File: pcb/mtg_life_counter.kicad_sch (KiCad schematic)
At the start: 41 parts, among them J1 USB C 4907, J2 ICSP, J3 TP_UART, SW1 SW_SPST, SW2 SW_SPST, U1 ATmega328P-AU, Y1 16MHz

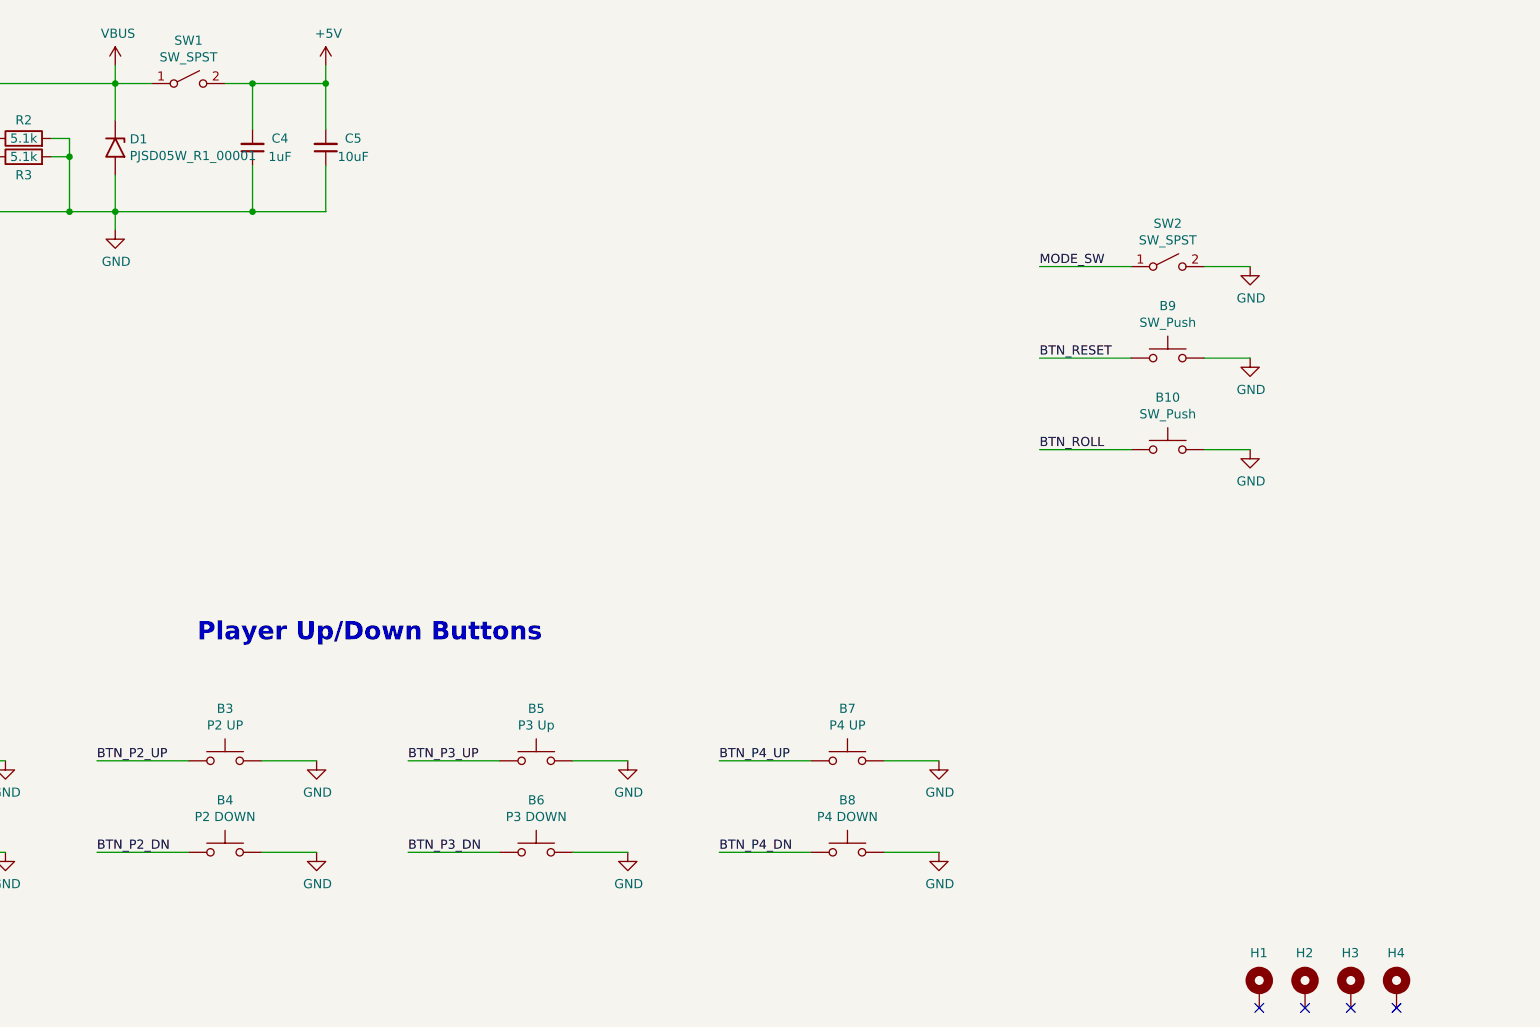
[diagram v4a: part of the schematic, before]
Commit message: start to route display traces
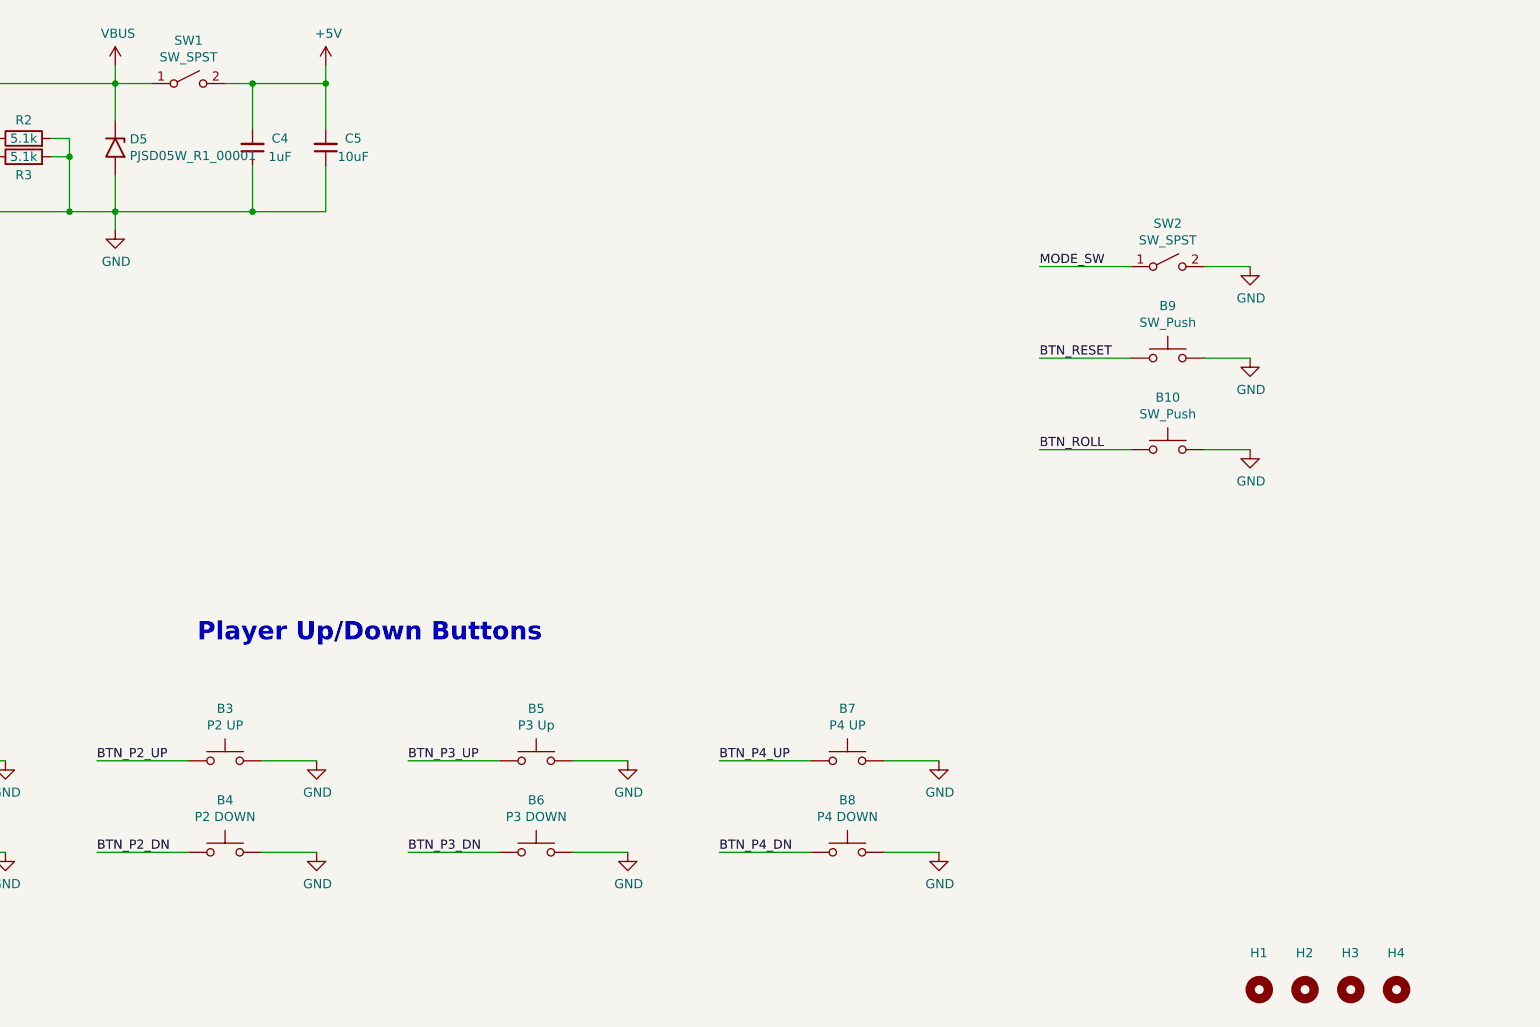
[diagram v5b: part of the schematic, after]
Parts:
- H1, H2, H3, H4: footprint MountingHole:MountingHole_3.2mm_M3_Pad_Via -> MountingHole:MountingHole_3.2mm_M3; symbol Mechanical:MountingHole_Pad -> Mechanical:MountingHole; now left out of the parts list
- renumbered D1 to D5
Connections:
- no-connect marks 8 -> 4
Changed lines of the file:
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@@
 	)
 	(no_connect
-		(at 243.84 255.27)
-	)
-	(no_connect
 		(at 69.85 78.74)
 	)
 	(no_connect
-		(at 256.54 255.27)
-	)
-	(no_connect
 		(at 69.85 76.2)
 	)
@@
 	)
 	(no_connect
-		(at 237.49 255.27)
-	)
-	(no_connect
 		(at 69.85 66.04)
 	)
-	(no_connect
-		(at 250.19 255.27)
-	)
 	(wire
 		(pts
@@
 	)
 	(symbol
-		(lib_id "Mechanical:MountingHole_Pad")
+		(lib_id "Mechanical:MountingHole")
 		(at 237.49 252.73 0)
 		(unit 1)
 		(exclude_from_sim no)
-		(in_bom yes)
+		(in_bom no)
 		(on_board yes)
 		(dnp no)
@@
 			)
 		)
-		(property "Footprint" "MountingHole:MountingHole_3.2mm_M3_Pad_Via"
+		(property "Footprint" "MountingHole:MountingHole_3.2mm_M3"
 			(at 237.49 252.73 0)
 			(effects
@@
 			)
 		)
-		(property "Description" ""
+		(property "Description" "Mounting Hole without connection"
 			(at 237.49 252.73 0)
 			(effects
@@
 			)
 		)
-		(pin "1"
-		)
 		(instances
 			(project "mtg_life_counter"
@@
 	)
 	(symbol
-		(lib_id "Mechanical:MountingHole_Pad")
+		(lib_id "Mechanical:MountingHole")
 		(at 256.54 252.73 0)
 		(unit 1)
 		(exclude_from_sim no)
-		(in_bom yes)
+		(in_bom no)
 		(on_board yes)
 		(dnp no)
@@
 			)
 		)
-		(property "Footprint" "MountingHole:MountingHole_3.2mm_M3_Pad_Via"
+		(property "Footprint" "MountingHole:MountingHole_3.2mm_M3"
 			(at 256.54 252.73 0)
 			(effects
@@
 			)
 		)
-		(property "Description" ""
+		(property "Description" "Mounting Hole without connection"
 			(at 256.54 252.73 0)
 			(effects
@@
 			)
 		)
-		(pin "1"
-		)
 		(instances
 			(project "mtg_life_counter"
@@
 	)
 	(symbol
-		(lib_id "Mechanical:MountingHole_Pad")
+		(lib_id "Mechanical:MountingHole")
 		(at 250.19 252.73 0)
 		(unit 1)
 		(exclude_from_sim no)
-		(in_bom yes)
+		(in_bom no)
 		(on_board yes)
 		(dnp no)
@@
 			)
 		)
-		(property "Footprint" "MountingHole:MountingHole_3.2mm_M3_Pad_Via"
+		(property "Footprint" "MountingHole:MountingHole_3.2mm_M3"
 			(at 250.19 252.73 0)
 			(effects
@@
 			)
 		)
-		(property "Description" ""
+		(property "Description" "Mounting Hole without connection"
 			(at 250.19 252.73 0)
 			(effects
@@
 			)
 		)
-		(pin "1"
-		)
 		(instances
 			(project "mtg_life_counter"
@@
 	)
 	(symbol
-		(lib_id "Mechanical:MountingHole_Pad")
+		(lib_id "Mechanical:MountingHole")
 		(at 243.84 252.73 0)
 		(unit 1)
 		(exclude_from_sim no)
-		(in_bom yes)
+		(in_bom no)
 		(on_board yes)
 		(dnp no)
@@
 			)
 		)
-		(property "Footprint" "MountingHole:MountingHole_3.2mm_M3_Pad_Via"
+		(property "Footprint" "MountingHole:MountingHole_3.2mm_M3"
 			(at 243.84 252.73 0)
 			(effects
@@
 			)
 		)
-		(property "Description" ""
+		(property "Description" "Mounting Hole without connection"
 			(at 243.84 252.73 0)
 			(effects
@@
 			)
 		)
-		(pin "1"
-		)
 		(instances
 			(project "mtg_life_counter"
@@
 		(on_board yes)
 		(dnp no)
-		(property "Reference" "D1"
+		(property "Reference" "D5"
 			(at 80.7466 134.7216 90)
 			(effects
@@
 			(project "mtg_life_counter"
 				(path "/1883df74-0bd5-446c-9076-f848bb3cfebf"
-					(reference "D1")
+					(reference "D5")
 					(unit 1)
 				)

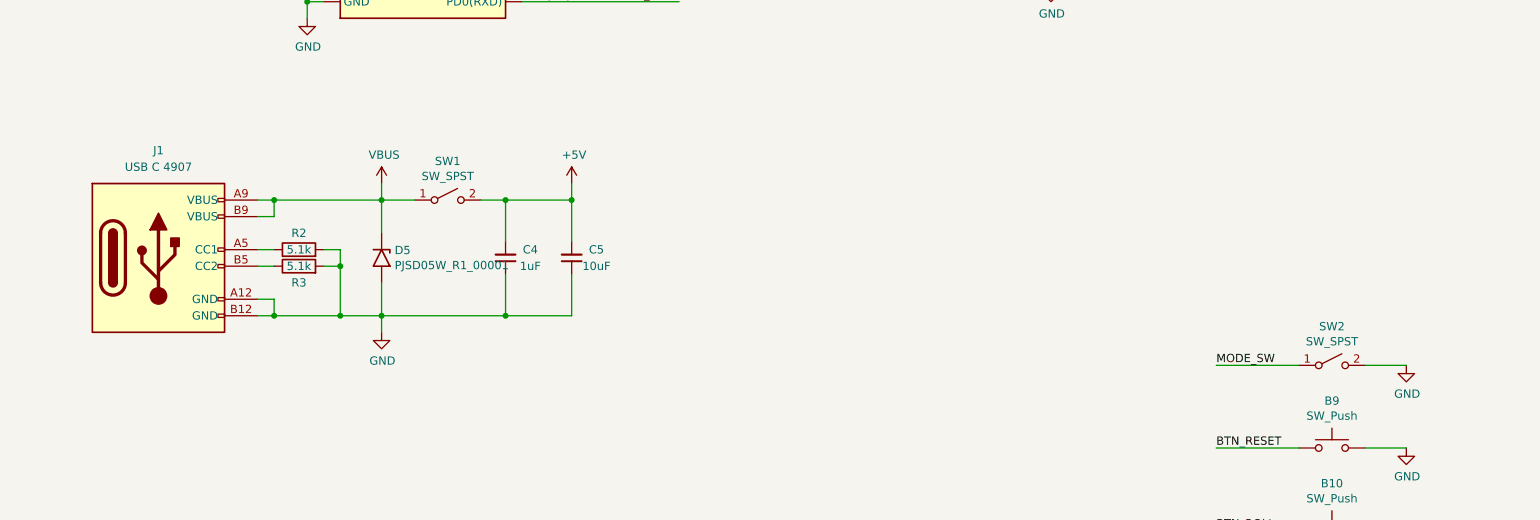
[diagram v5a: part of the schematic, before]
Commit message: switch to all smd components
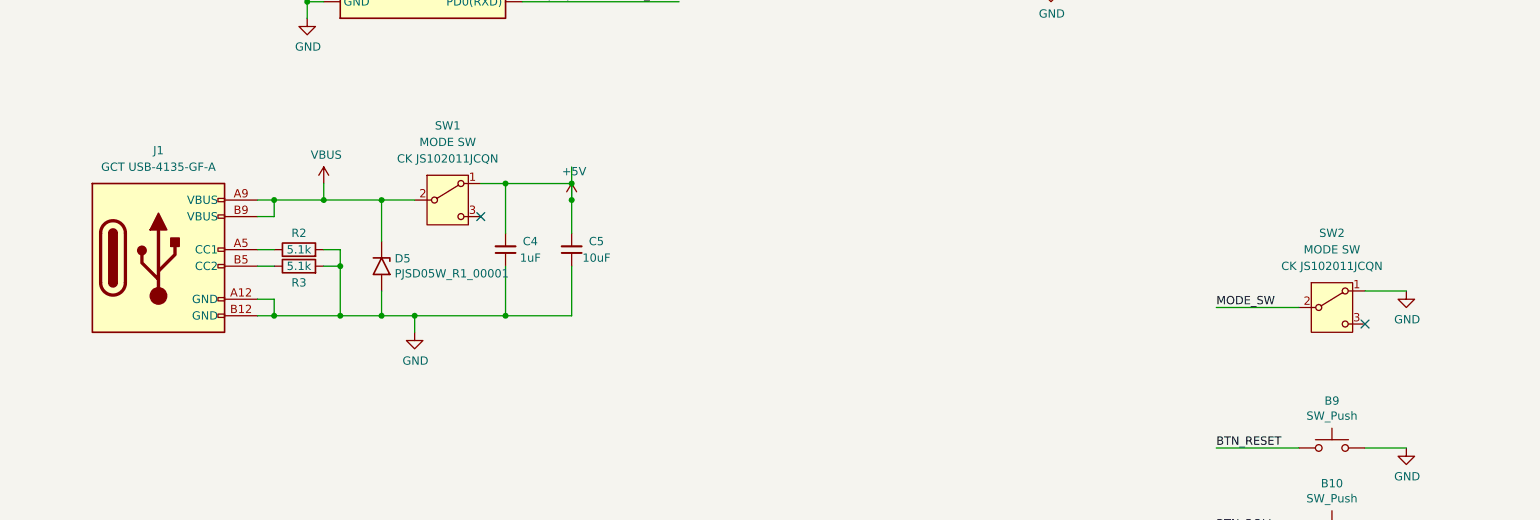
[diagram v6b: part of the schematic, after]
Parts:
- removed SW1, SW2: SW_SPST, Button_Switch_THT:SW_Slide_SPDT_Straight_CK_OS102011MS2Q, symbol Switch:SW_SPST
- added SW1, SW2: MODE SW, mtg_life_counter:SW_SPDT_CK_JS102011JCQN, symbol Switch:SW_SPDT
- B1, B10, B2, B3, B4, B5, B6, B7, B8, B9: footprint mtg_life_counter:B3F_12mm -> mtg_life_counter:SW_SPST_WE_WS-TASV_12mm_Tac
- J1: value USB C 4907 -> GCT USB-4135-GF-A; footprint mtg_life_counter:4907_USB_C_PowerOnly -> Connector_USB:USB_C_Receptacle_GCT_USB4135-GF-A_6P_TopMnt_Horizontal
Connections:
- net +5V: now also SW1.1 (A)
- net GND: now also SW2.1 (A)
- net MODE_SW: now also SW2.2 (B)
- net VBUS: now also SW1.2 (B)
- no-connect marks 4 -> 6
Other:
- moved on the sheet: C4, C5, D5

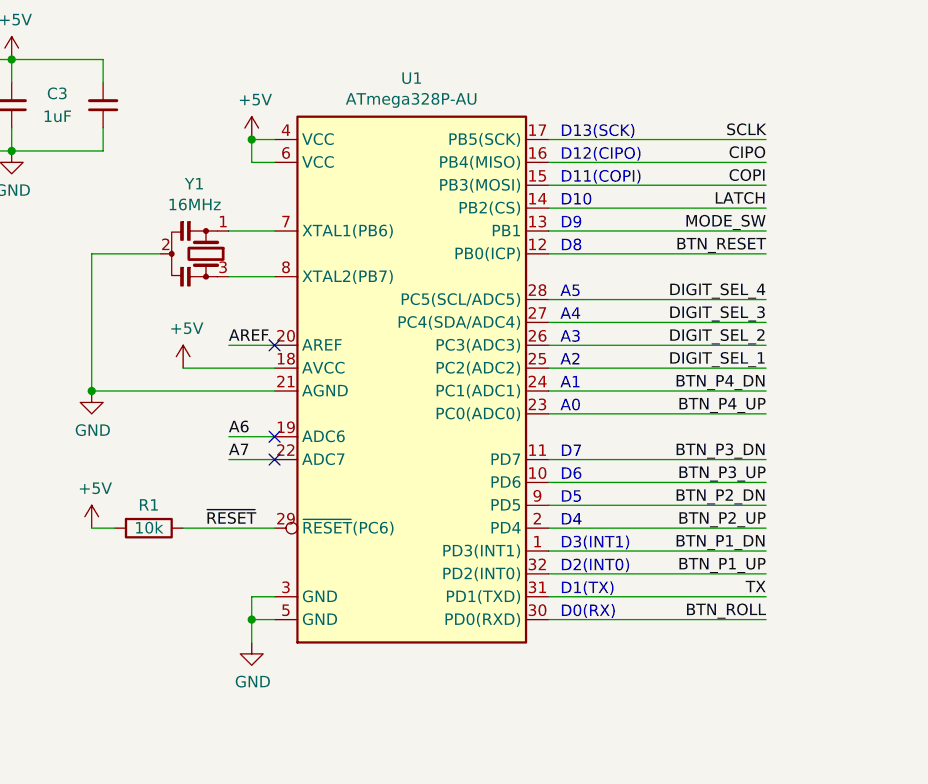
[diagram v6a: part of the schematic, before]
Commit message: continue layout. improve 3d model
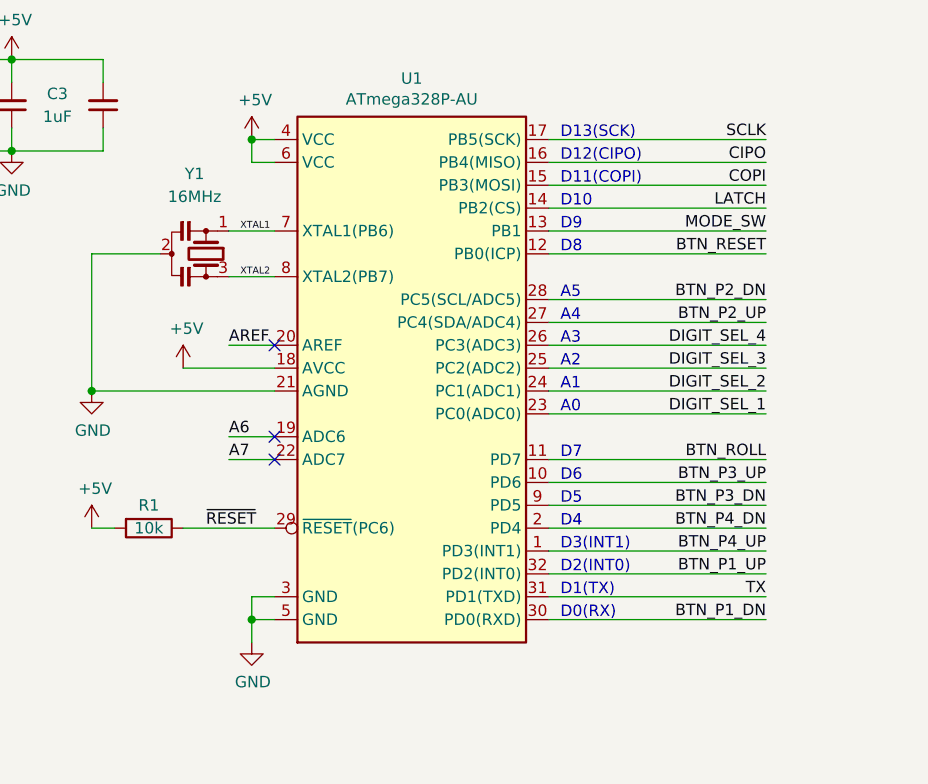
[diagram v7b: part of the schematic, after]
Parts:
- Y1: footprint Crystal:Resonator_SMD-3Pin_7.2x3.0mm -> Crystal:Resonator_SMD_Murata_CSTxExxV-3Pin_3.0x1.1mm_HandSoldering
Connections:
- net BTN_P1_DN: now also U1.30 (PD0(RXD)); no longer U1.1 (PD3(INT1))
- net BTN_P2_DN: now also U1.28 (PC5(SCL/ADC5)); no longer U1.9 (PD5)
- net BTN_P2_UP: now also U1.27 (PC4(SDA/ADC4)); no longer U1.2 (PD4)
- net BTN_P3_DN: now also U1.9 (PD5); no longer U1.11 (PD7)
- net BTN_P4_DN: now also U1.2 (PD4); no longer U1.24 (PC1(ADC1))
- net BTN_P4_UP: now also U1.1 (PD3(INT1)); no longer U1.23 (PC0(ADC0))
- net BTN_ROLL: now also U1.11 (PD7); no longer U1.30 (PD0(RXD))
- net DIGIT_SEL_1: now also U1.23 (PC0(ADC0)); no longer U1.25 (PC2(ADC2))
- net DIGIT_SEL_2: now also U1.24 (PC1(ADC1)); no longer U1.26 (PC3(ADC3))
- net DIGIT_SEL_3: now also U1.25 (PC2(ADC2)); no longer U1.27 (PC4(SDA/ADC4))
- net DIGIT_SEL_4: now also U1.26 (PC3(ADC3)); no longer U1.28 (PC5(SCL/ADC5))
- net XTAL1: now reaches U1.7 (XTAL1(PB6)), Y1.1
- net XTAL2: now reaches U1.8 (XTAL2(PB7)), Y1.3
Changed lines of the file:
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@@
 	)
 	(label "BTN_P1_DN"
-		(at 124.46 88.9 180)
+		(at 124.46 96.52 180)
 		(effects
 			(font
@@
 	)
 	(label "BTN_P2_UP"
-		(at 124.46 86.36 180)
+		(at 124.46 63.5 180)
 		(effects
 			(font
@@
 	)
 	(label "DIGIT_SEL_3"
-		(at 124.46 63.5 180)
+		(at 124.46 68.58 180)
 		(effects
 			(font
@@
 	)
 	(label "BTN_P4_DN"
-		(at 124.46 71.12 180)
+		(at 124.46 86.36 180)
 		(effects
 			(font
@@
 	)
 	(label "DIGIT_SEL_1"
-		(at 124.46 68.58 180)
+		(at 124.46 73.66 180)
 		(effects
 			(font
@@
 		)
 	)
+	(label "XTAL2"
+		(at 66.04 58.42 0)
+		(effects
+			(font
+				(size 0.762 0.762)
+			)
+			(justify left bottom)
+		)
+	)
 	(label "LATCH"
 		(at 314.96 147.32 0)
@@
 	)
 	(label "DIGIT_SEL_4"
-		(at 124.46 60.96 180)
+		(at 124.46 66.04 180)
 		(effects
 			(font
@@
 		)
 	)
+	(label "XTAL1"
+		(at 66.04 53.34 0)
+		(effects
+			(font
+				(size 0.762 0.762)
+			)
+			(justify left bottom)
+		)
+	)
 	(label "BTN_P4_DN"
 		(at 162.56 233.68 0)
@@
 	)
 	(label "BTN_ROLL"
-		(at 124.46 96.52 180)
+		(at 124.46 78.74 180)
 		(effects
 			(font
@@
 	)
 	(label "BTN_P4_UP"
-		(at 124.46 73.66 180)
+		(at 124.46 88.9 180)
 		(effects
 			(font
@@
 	)
 	(label "BTN_P3_DN"
-		(at 124.46 78.74 180)
+		(at 124.46 83.82 180)
 		(effects
 			(font
@@
 	)
 	(label "BTN_P2_DN"
-		(at 124.46 83.82 180)
+		(at 124.46 60.96 180)
 		(effects
 			(font
@@
 	)
 	(label "DIGIT_SEL_2"
-		(at 124.46 66.04 180)
+		(at 124.46 71.12 180)
 		(effects
 			(font
@@
 		(dnp no)
 		(property "Reference" "Y1"
-			(at 60.96 48.133 90)
+			(at 60.96 46.99 90)
 			(effects
 				(font
@@
 		)
 		(property "Value" "16MHz"
-			(at 60.96 50.4444 90)
-			(effects
-				(font
-					(size 1.27 1.27)
-				)
-			)
-		)
-		(property "Footprint" "Crystal:Resonator_SMD-3Pin_7.2x3.0mm"
+			(at 60.96 49.53 90)
+			(effects
+				(font
+					(size 1.27 1.27)
+				)
+			)
+		)
+		(property "Footprint" "Crystal:Resonator_SMD_Murata_CSTxExxV-3Pin_3.0x1.1mm_HandSoldering"
 			(at 62.23 55.245 0)
 			(effects
